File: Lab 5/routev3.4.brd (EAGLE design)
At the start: 100 x 80 mm, 48 parts, among them J1 FTDI_DEVICERA_SMT, M1 WIRELESS-NRF24L01, U1 3.3V, U2 GY-521MPU6050

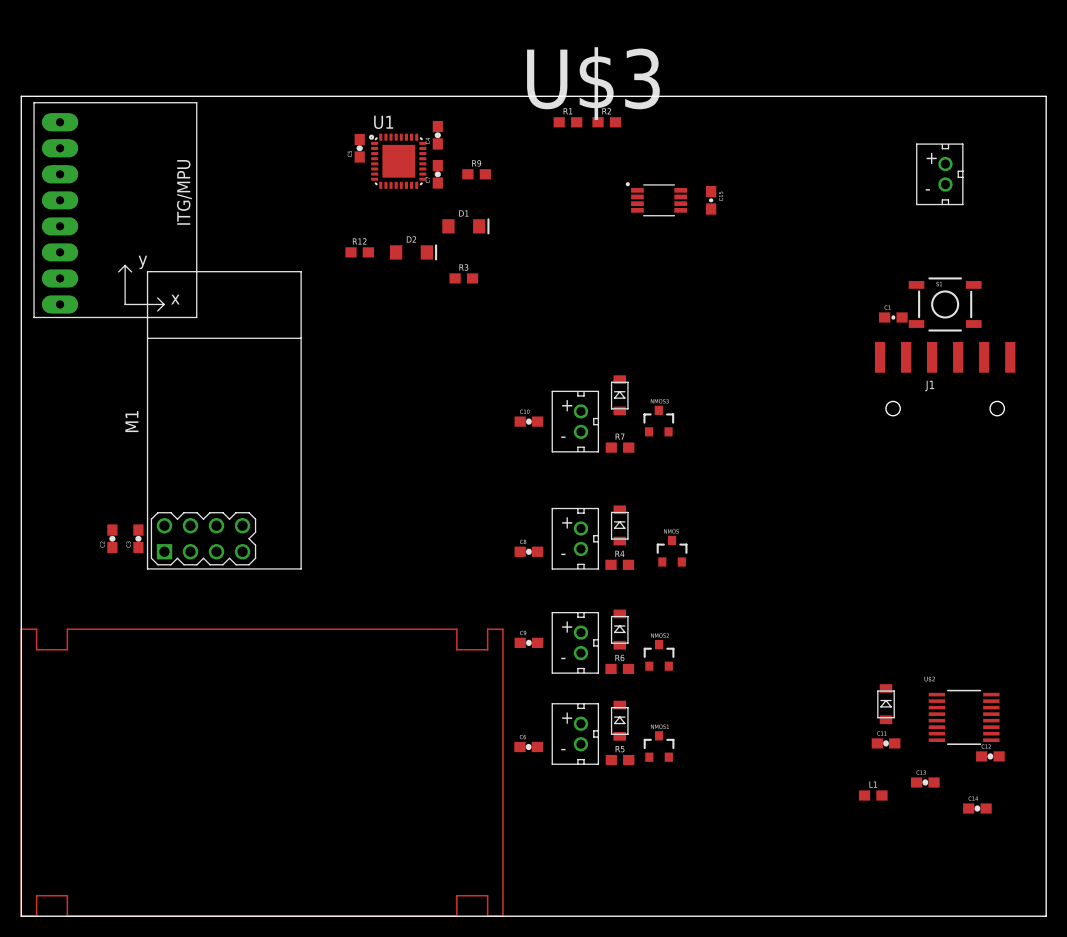
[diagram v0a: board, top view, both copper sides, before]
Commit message: Update template for cut-out - Latest route: routev3.5_vccgnd
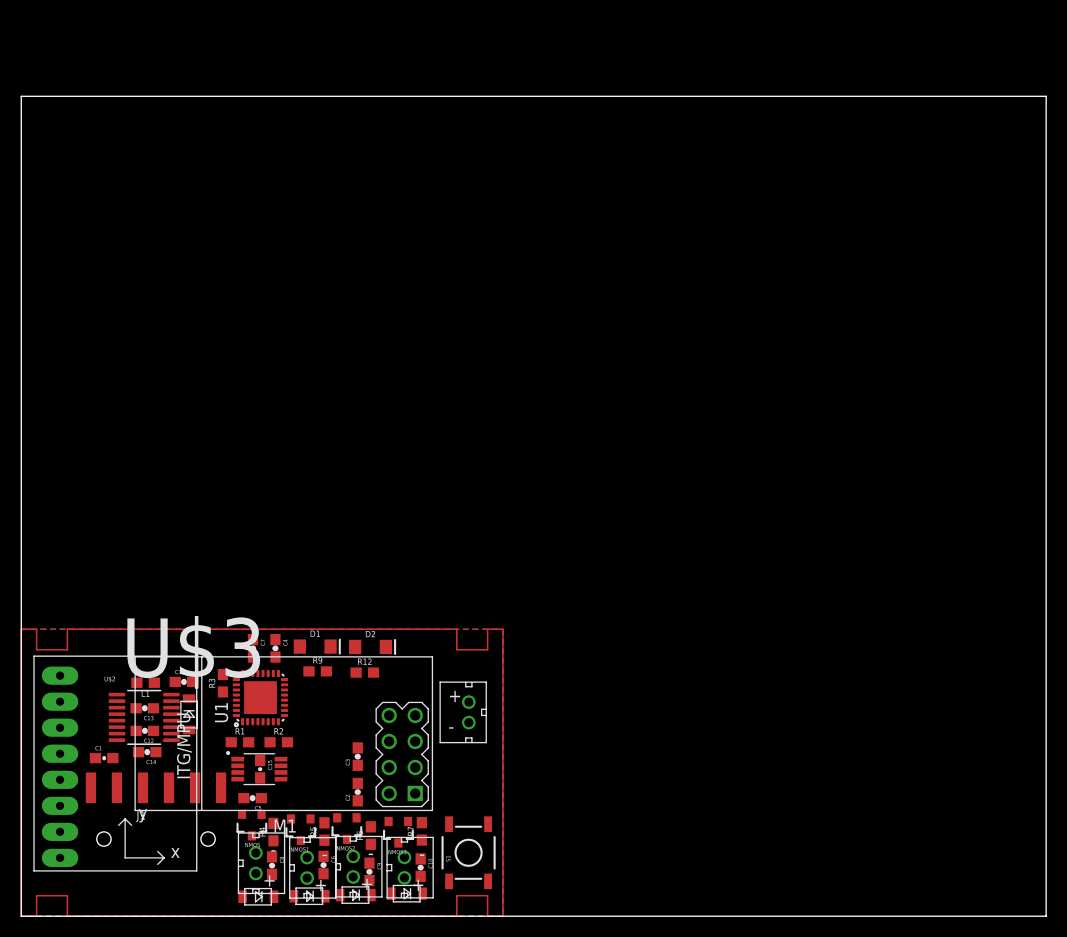
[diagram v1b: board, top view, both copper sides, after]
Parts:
- moved C1 88.2 mm to (8.09, 15.4)
- moved J1 87.7 mm to (13.1, 7.53)
- moved C12 82.5 mm to (12.1, 18.1), turned to 180 degrees
- moved C14 81.2 mm to (12.3, 16.0), turned to 180 degrees
- moved U$2 80.0 mm to (12.0, 19.4)
- moved C13 76.5 mm to (12.1, 20.3), turned to 180 degrees
- moved L1 71.8 mm to (12.1, 22.8), turned to 180 degrees
- moved S1 70.9 mm to (43.6, 6.19), turned to 90 degrees
- moved C15 70.8 mm to (23.3, 14.3)
- moved U$1 70.1 mm to (43.7, 19.9)
- moved C11 68.8 mm to (15.9, 22.9)
- moved R1 68.4 mm to (21.3, 17.0)
- moved R2 68.4 mm to (25.1, 17.0)
- moved DIODE4 68.0 mm to (16.4, 19.7)
- moved U$3 67.8 mm to (23.2, 14.3)
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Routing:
- added copper zone on layer 1, net BATTERY_+
- added copper zone on layer 16, net GND
